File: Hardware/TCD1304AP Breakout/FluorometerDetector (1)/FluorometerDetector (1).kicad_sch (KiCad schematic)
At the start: 7 parts

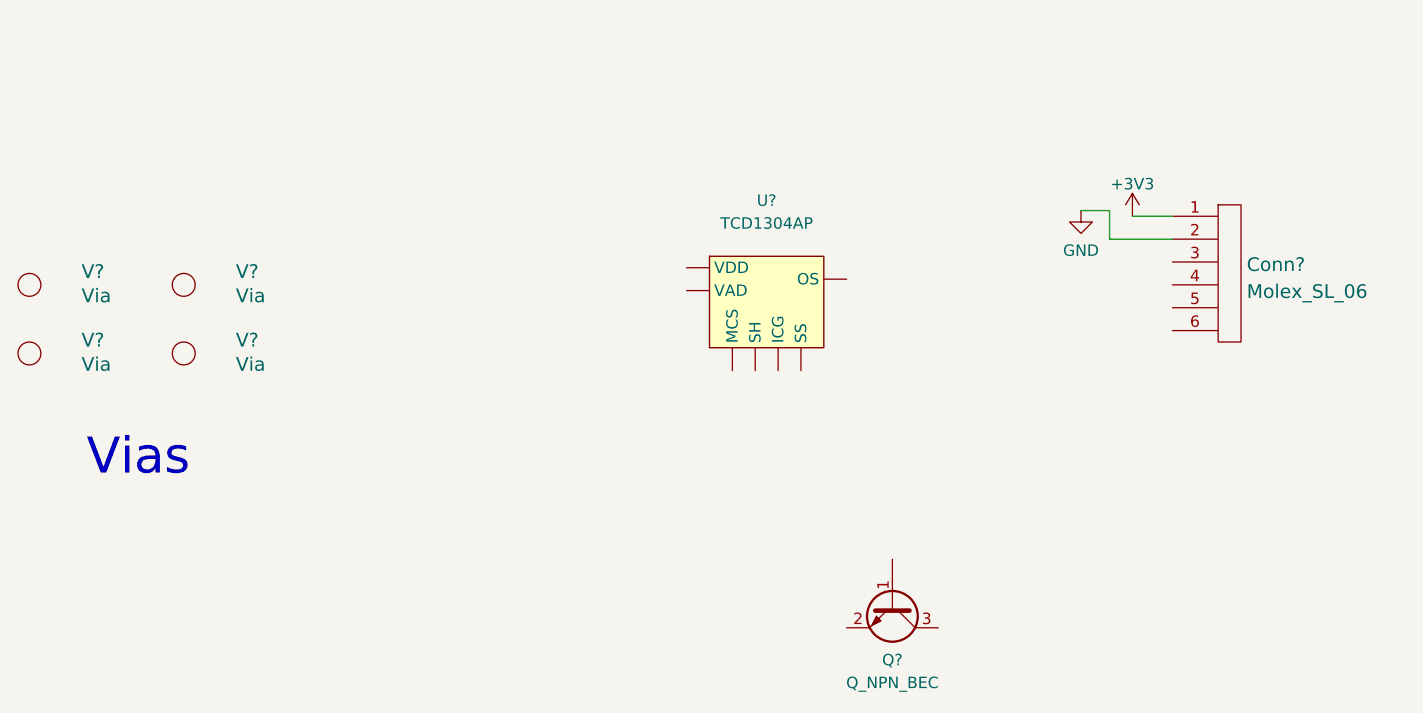
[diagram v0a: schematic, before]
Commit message: Layout updated for LEDs and Science Sensor Board, schematic for CCD
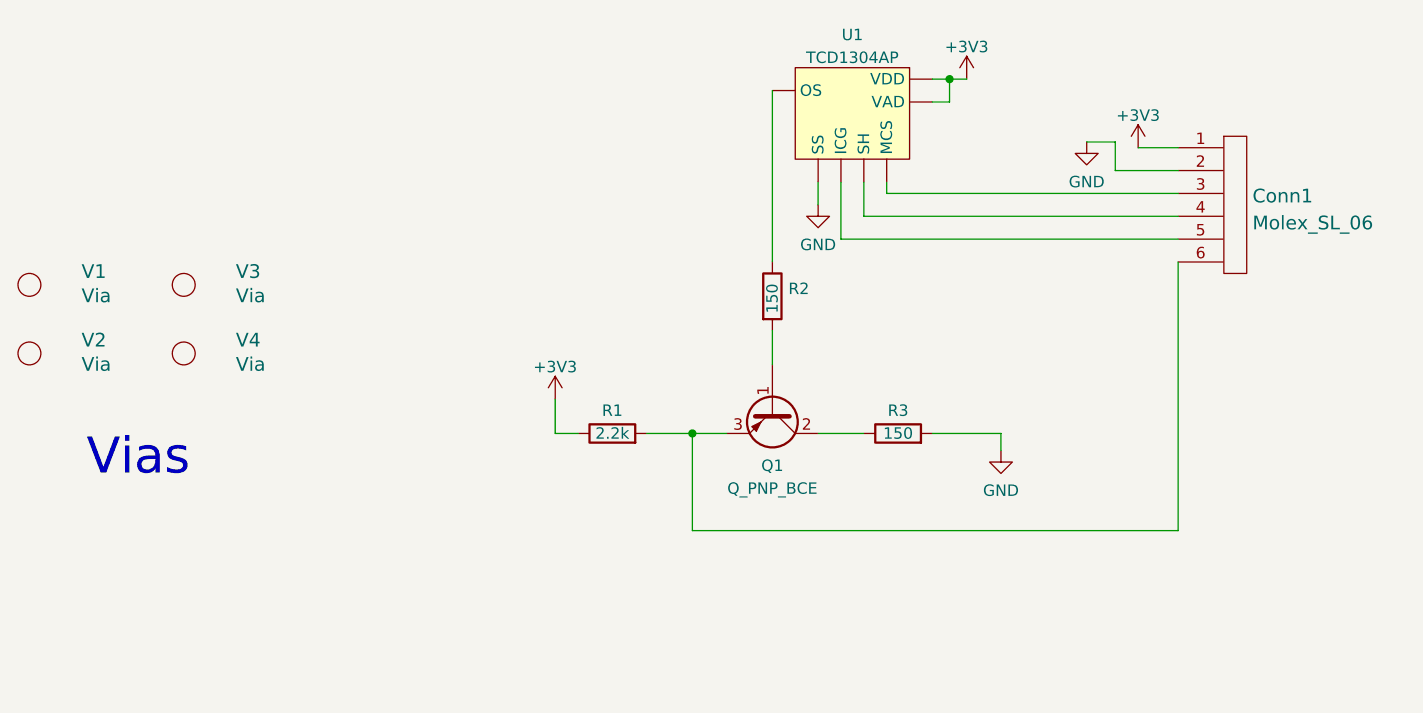
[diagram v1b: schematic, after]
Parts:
- removed Q?: Q_NPN_BEC, symbol Device:Q_NPN_BEC
- added Q1: Q_PNP_BCE, symbol Device:Q_PNP_BCE
- added R1: 2.2k, symbol Device:R
- added R2, R3: 150, symbol Device:R
- gave numbers to parts that had none: 6
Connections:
- net +3V3: now also U1. (VDD), R1.1
- net GND: now also U1. (VDD), R3.2
- net at Conn1.3: now also U1. (VDD)
- net at Conn1.4: now also U1. (VDD)
- net at Conn1.5: now also U1. (VDD)
- net at Conn1.6: now also Q1.3 (E), R1.2
- new net: R2.1, U1. (VDD)
- new net: Q1.1 (B), R2.2
- new net: Q1.2 (C), R3.1
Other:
- moved on the sheet: Conn1, U1

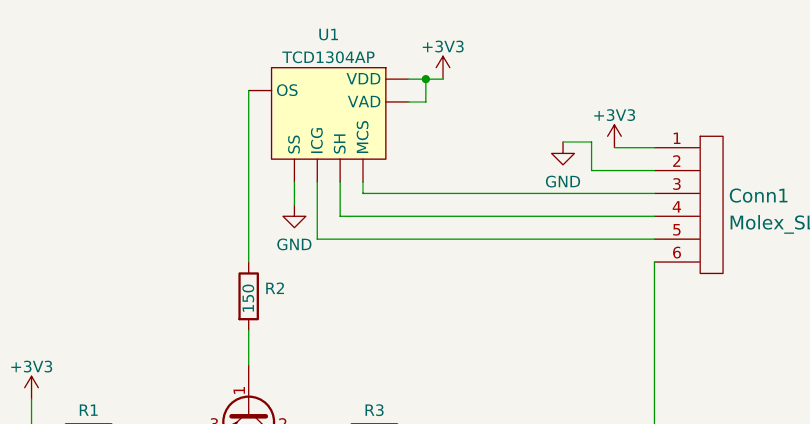
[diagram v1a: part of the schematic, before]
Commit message: Found footprint for CCD
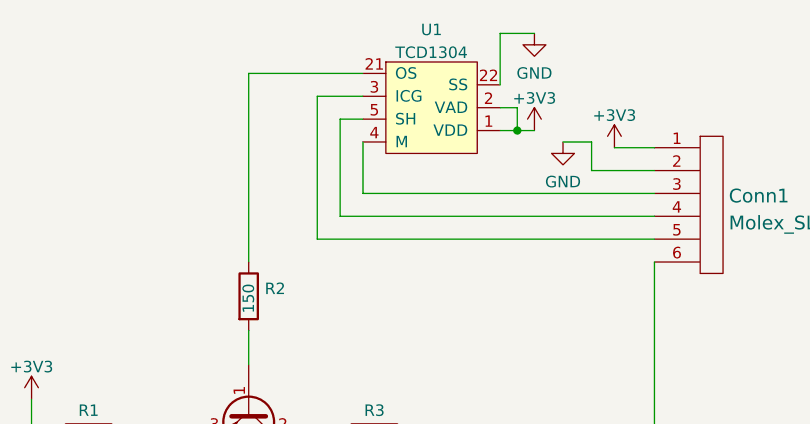
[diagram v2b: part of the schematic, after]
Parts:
- removed U1: TCD1304AP, symbol TCD1304AP:TCD1304AP
- added U1: TCD1304, UVLEDs:DIP1016W62P254L4160H372Q22N, symbol MRDT_Sensors:TCD1304
- Conn1: footprint (none) -> UVLEDs:705550040
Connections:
- net +3V3: now also U1.1 (VDD), U1.2 (VAD)
- net GND: now also U1.22 (SS)
- net at R2.1: now also U1.21 (OS)
- net at Conn1.3: now also U1.4 (M)
- net at Conn1.4: now also U1.5 (SH)
- net at Conn1.5: now also U1.3 (ICG)
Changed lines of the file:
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@@
 (kicad_sch (version 20211123) (generator eeschema)
   (paper "A4")
-  (junction (at 159.385 25.4) (diameter 0) (color 0 0 0 0)
-  )
   (junction (at 130.81 64.77) (diameter 0) (color 0 0 0 0)
   )
+  (junction (at 169.545 31.115) (diameter 0) (color 0 0 0 0)
+  )
   (wire (pts (xy 177.8 35.56) (xy 177.8 32.385))
     (stroke (width 0) (type default) (color 0 0 0 0))
@@
     (stroke (width 0) (type default) (color 0 0 0 0))
   )
-  (wire (pts (xy 149.86 40.64) (xy 149.86 36.83))
+  (wire (pts (xy 149.86 29.845) (xy 149.86 40.64))
     (stroke (width 0) (type default) (color 0 0 0 0))
   )
@@
     (stroke (width 0) (type default) (color 0 0 0 0))
   )
-  (wire (pts (xy 147.32 43.18) (xy 147.32 36.83))
+  (wire (pts (xy 147.32 27.305) (xy 147.32 43.18))
     (stroke (width 0) (type default) (color 0 0 0 0))
   )
@@
     (stroke (width 0) (type default) (color 0 0 0 0))
   )
+  (wire (pts (xy 152.4 27.305) (xy 147.32 27.305))
+    (stroke (width 0) (type default) (color 0 0 0 0))
+  )
   (wire (pts (xy 184.785 38.1) (xy 152.4 38.1))
     (stroke (width 0) (type default) (color 0 0 0 0))
@@
     (stroke (width 0) (type default) (color 0 0 0 0))
   )
-  (wire (pts (xy 159.385 27.94) (xy 159.385 25.4))
+  (wire (pts (xy 152.4 24.765) (xy 139.7 24.765))
+    (stroke (width 0) (type default) (color 0 0 0 0))
+  )
+  (wire (pts (xy 152.4 32.385) (xy 152.4 38.1))
+    (stroke (width 0) (type default) (color 0 0 0 0))
+  )
+  (wire (pts (xy 169.545 31.115) (xy 169.545 28.575))
     (stroke (width 0) (type default) (color 0 0 0 0))
   )
@@
     (stroke (width 0) (type default) (color 0 0 0 0))
   )
-  (wire (pts (xy 139.7 45.72) (xy 139.7 26.67))
+  (wire (pts (xy 139.7 24.765) (xy 139.7 45.72))
     (stroke (width 0) (type default) (color 0 0 0 0))
   )
@@
     (stroke (width 0) (type default) (color 0 0 0 0))
   )
-  (wire (pts (xy 152.4 38.1) (xy 152.4 36.83))
-    (stroke (width 0) (type default) (color 0 0 0 0))
-  )
-  (wire (pts (xy 159.385 25.4) (xy 161.29 25.4))
-    (stroke (width 0) (type default) (color 0 0 0 0))
-  )
-  (wire (pts (xy 159.385 27.94) (xy 157.48 27.94))
+  (wire (pts (xy 169.545 31.115) (xy 171.45 31.115))
+    (stroke (width 0) (type default) (color 0 0 0 0))
+  )
+  (wire (pts (xy 169.545 31.115) (xy 167.64 31.115))
     (stroke (width 0) (type default) (color 0 0 0 0))
   )
@@
     (stroke (width 0) (type default) (color 0 0 0 0))
   )
+  (wire (pts (xy 167.64 20.32) (xy 167.64 26.035))
+    (stroke (width 0) (type default) (color 0 0 0 0))
+  )
+  (wire (pts (xy 152.4 29.845) (xy 149.86 29.845))
+    (stroke (width 0) (type default) (color 0 0 0 0))
+  )
   (wire (pts (xy 139.7 53.34) (xy 139.7 57.15))
     (stroke (width 0) (type default) (color 0 0 0 0))
@@
     (stroke (width 0) (type default) (color 0 0 0 0))
   )
-  (wire (pts (xy 144.78 36.83) (xy 144.78 39.37))
-    (stroke (width 0) (type default) (color 0 0 0 0))
-  )
-  (wire (pts (xy 159.385 25.4) (xy 157.48 25.4))
+  (wire (pts (xy 169.545 28.575) (xy 167.64 28.575))
     (stroke (width 0) (type default) (color 0 0 0 0))
   )
@@
   )
   (wire (pts (xy 177.8 32.385) (xy 174.625 32.385))
+    (stroke (width 0) (type default) (color 0 0 0 0))
+  )
+  (wire (pts (xy 171.45 20.32) (xy 167.64 20.32))
     (stroke (width 0) (type default) (color 0 0 0 0))
   )
@@
     (pin "1")
   )
-  (symbol (lib_id "power:GND") (at 144.78 39.37 0) (unit 1)
-    (in_bom yes) (on_board yes) (fields_autoplaced)
-    (property "Reference" "#PWR02" (id 0) (at 144.78 45.72 0)
-      (effects (font (size 1.27 1.27)) hide)
-    )
-    (property "Value" "GND" (id 1) (at 144.78 43.8134 0))
-    (property "Footprint" "" (id 2) (at 144.78 39.37 0)
-      (effects (font (size 1.27 1.27)) hide)
-    )
-    (property "Datasheet" "" (id 3) (at 144.78 39.37 0)
+  (symbol (lib_id "power:GND") (at 171.45 20.32 0) (unit 1)
+    (in_bom yes) (on_board yes) (fields_autoplaced)
+    (property "Reference" "#PWR02" (id 0) (at 171.45 26.67 0)
+      (effects (font (size 1.27 1.27)) hide)
+    )
+    (property "Value" "GND" (id 1) (at 171.45 24.7634 0))
+    (property "Footprint" "" (id 2) (at 171.45 20.32 0)
+      (effects (font (size 1.27 1.27)) hide)
+    )
+    (property "Datasheet" "" (id 3) (at 171.45 20.32 0)
       (effects (font (size 1.27 1.27)) hide)
     )
@@
     (pin "1")
   )
-  (symbol (lib_id "power:+3V3") (at 161.29 25.4 0) (unit 1)
-    (in_bom yes) (on_board yes) (fields_autoplaced)
-    (property "Reference" "#PWR03" (id 0) (at 161.29 29.21 0)
-      (effects (font (size 1.27 1.27)) hide)
-    )
-    (property "Value" "+3V3" (id 1) (at 161.29 21.8242 0))
-    (property "Footprint" "" (id 2) (at 161.29 25.4 0)
-      (effects (font (size 1.27 1.27)) hide)
-    )
-    (property "Datasheet" "" (id 3) (at 161.29 25.4 0)
+  (symbol (lib_id "power:+3V3") (at 171.45 31.115 0) (unit 1)
+    (in_bom yes) (on_board yes) (fields_autoplaced)
+    (property "Reference" "#PWR03" (id 0) (at 171.45 34.925 0)
+      (effects (font (size 1.27 1.27)) hide)
+    )
+    (property "Value" "+3V3" (id 1) (at 171.45 27.5392 0))
+    (property "Footprint" "" (id 2) (at 171.45 31.115 0)
+      (effects (font (size 1.27 1.27)) hide)
+    )
+    (property "Datasheet" "" (id 3) (at 171.45 31.115 0)
       (effects (font (size 1.27 1.27)) hide)
     )
@@
     (pin "2")
   )
+  (symbol (lib_id "MRDT_Sensors:TCD1304") (at 165.1 23.495 180) (unit 1)
+    (in_bom yes) (on_board yes)
+    (property "Reference" "U1" (id 0) (at 160.02 19.9222 0))
+    (property "Value" "TCD1304" (id 1) (at 160.02 22.4591 0))
+    (property "Footprint" "UVLEDs:DIP1016W62P254L4160H372Q22N" (id 2) (at 172.72 10.795 0)
+      (effects (font (size 1.27 1.27)) hide)
+    )
+    (property "Datasheet" "" (id 3) (at 172.72 10.795 0)
+      (effects (font (size 1.27 1.27)) hide)
+    )
+    (pin "1")
+    (pin "2")
+    (pin "21")
+    (pin "22")
+    (pin "3")
+    (pin "4")
+    (pin "5")
+  )
   (symbol (lib_id "MRDT_Drill_Holes:Via") (at 74.295 55.88 0) (unit 1)
     (in_bom yes) (on_board yes)
@@
     (pin "1")
   )
-  (symbol (lib_id "TCD1304AP:TCD1304AP") (at 148.59 29.21 0) (mirror y) (unit 1)
-    (in_bom yes) (on_board yes) (fields_autoplaced)
-    (property "Reference" "U1" (id 0) (at 148.59 20.481 0))
-    (property "Value" "TCD1304AP" (id 1) (at 148.59 23.0179 0))
-    (property "Footprint" "" (id 2) (at 148.59 29.21 0)
-      (effects (font (size 1.27 1.27)) hide)
-    )
-    (property "Datasheet" "" (id 3) (at 148.59 29.21 0)
-      (effects (font (size 1.27 1.27)) hide)
-    )
-    (pin "")
-    (pin "")
-    (pin "")
-    (pin "")
-    (pin "")
-    (pin "")
-    (pin "")
-  )
   (symbol (lib_id "MRDT_Drill_Holes:Via") (at 57.15 55.88 0) (unit 1)
     (in_bom yes) (on_board yes)
@@
       (effects (font (size 1.524 1.524)) (justify left))
     )
-    (property "Footprint" "" (id 2) (at 189.865 44.45 0)
+    (property "Footprint" "UVLEDs:705550040" (id 2) (at 189.865 44.45 0)
       (effects (font (size 1.524 1.524)) hide)
     )
@@
     )
     (path "/fa5d2e23-cb22-43d6-9b2d-b288e81d34e5"
-      (reference "Conn1") (unit 1) (value "Molex_SL_06") (footprint "")
+      (reference "Conn1") (unit 1) (value "Molex_SL_06") (footprint "UVLEDs:705550040")
     )
     (path "/b0e93359-de99-4c71-ac67-db20d611c11c"
@@
       (reference "R3") (unit 1) (value "150") (footprint "")
     )
-    (path "/cc8a3a98-da51-4eb3-bcfd-21ea57c191f1"
-      (reference "U1") (unit 1) (value "TCD1304AP") (footprint "")
+    (path "/7b7d6c50-0f51-4d1e-926c-e78a7fc8517e"
+      (reference "U1") (unit 1) (value "TCD1304") (footprint "UVLEDs:DIP1016W62P254L4160H372Q22N")
     )
     (path "/e8448a02-52d5-4c3d-af6b-5aafb20d0ba8"
